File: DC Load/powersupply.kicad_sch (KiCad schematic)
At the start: 17 parts, among them IC2 LTC1046CS8#PBF, J4 DC 15V..18V, U10 MC7805BD2TR4G, U9 MC7812BD2TR4G

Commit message: Add 2.048 ref
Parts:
- added C?: 1uF, symbol Device:C_Polarized
- added C?: 10uF, symbol Device:C_Polarized
- added R?: 1K, symbol Device:R
- added R?: 470K, symbol Device:R
- added RV?: 10K, symbol Device:R_Potentiometer_Trim
- added TP?: +2.048V, symbol Connector:TestPoint
- added U?: REF5020AID, Package_SO:SOIC-8_3.9x4.9mm_P1.27mm, symbol Reference_Voltage:REF5020ID
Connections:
- net +5V: now also C?.1, U?.2 (Vin)
- new net: C?.2, C?.2, R?.1, U?.4 (GND)
- new net: R?.2, RV?.1
- new net: R?.2, RV?.2
- new net: R?.1, U?.5 (Trim/NR)
- new net +2.048V: C?.1, RV?.3, TP?.1, U?.6 (Vout)
- no-connect marks 3 -> 4

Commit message: update
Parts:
- gave numbers to parts that had none: 7
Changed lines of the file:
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@@
   (symbol (lib_id "Device:C_Polarized") (at 180.34 104.14 0) (unit 1)
     (in_bom yes) (on_board yes)
-    (property "Reference" "C?" (id 0) (at 181.61 101.6 0)
+    (property "Reference" "C10" (id 0) (at 181.61 101.6 0)
       (effects (font (size 1.27 1.27)) (justify left))
     )
@@
   (symbol (lib_id "Connector:TestPoint") (at 233.68 95.25 0) (unit 1)
     (in_bom yes) (on_board yes)
-    (property "Reference" "TP?" (id 0) (at 232.41 87.63 0)
+    (property "Reference" "TP8" (id 0) (at 232.41 87.63 0)
       (effects (font (size 1.27 1.27)) (justify left))
     )
@@
   (symbol (lib_id "Ben:+2.048V") (at 242.57 93.98 0) (unit 1)
     (in_bom yes) (on_board yes)
-    (property "Reference" "#PWR?" (id 0) (at 242.57 97.79 0)
+    (property "Reference" "#PWR09" (id 0) (at 242.57 97.79 0)
       (effects (font (size 1.27 1.27)) hide)
     )
@@
   (symbol (lib_id "Device:R") (at 228.6 115.57 180) (unit 1)
     (in_bom yes) (on_board yes)
-    (property "Reference" "R?" (id 0) (at 231.14 114.3 0))
+    (property "Reference" "R27" (id 0) (at 231.14 114.3 0))
     (property "Value" "1K" (id 1) (at 231.14 116.84 0))
     (property "Footprint" "" (id 2) (at 230.378 115.57 90)
@@
   (symbol (lib_id "Device:R_Potentiometer_Trim") (at 228.6 105.41 180) (unit 1)
     (in_bom yes) (on_board yes) (fields_autoplaced)
-    (property "Reference" "RV?" (id 0) (at 231.14 104.1399 0)
+    (property "Reference" "RV2" (id 0) (at 231.14 104.1399 0)
       (effects (font (size 1.27 1.27)) (justify right))
     )
@@
   (symbol (lib_id "Device:C_Polarized") (at 242.57 110.49 0) (unit 1)
     (in_bom yes) (on_board yes)
-    (property "Reference" "C?" (id 0) (at 243.84 107.95 0)
+    (property "Reference" "C11" (id 0) (at 243.84 107.95 0)
       (effects (font (size 1.27 1.27)) (justify left))
     )
@@
   (symbol (lib_id "power:+5V") (at 195.58 88.9 0) (unit 1)
     (in_bom yes) (on_board yes) (fields_autoplaced)
-    (property "Reference" "#PWR?" (id 0) (at 195.58 92.71 0)
+    (property "Reference" "#PWR08" (id 0) (at 195.58 92.71 0)
       (effects (font (size 1.27 1.27)) hide)
     )
@@
   (symbol (lib_id "Device:R") (at 218.44 105.41 90) (unit 1)
     (in_bom yes) (on_board yes)
-    (property "Reference" "R?" (id 0) (at 218.44 102.87 90))
+    (property "Reference" "R26" (id 0) (at 218.44 102.87 90))
     (property "Value" "470K" (id 1) (at 218.44 107.95 90))
     (property "Footprint" "" (id 2) (at 218.44 107.188 90)
@@
   (symbol (lib_id "Reference_Voltage:REF5020ID") (at 198.12 102.87 0) (unit 1)
     (in_bom yes) (on_board yes) (fields_autoplaced)
-    (property "Reference" "U?" (id 0) (at 197.5994 92.71 0)
-      (effects (font (size 1.27 1.27)) (justify left))
-    )
+    (property "Reference" "U5" (id 0) (at 197.5994 92.71 0)
+      (effects (font (size 1.27 1.27)) (justify left))
+    )

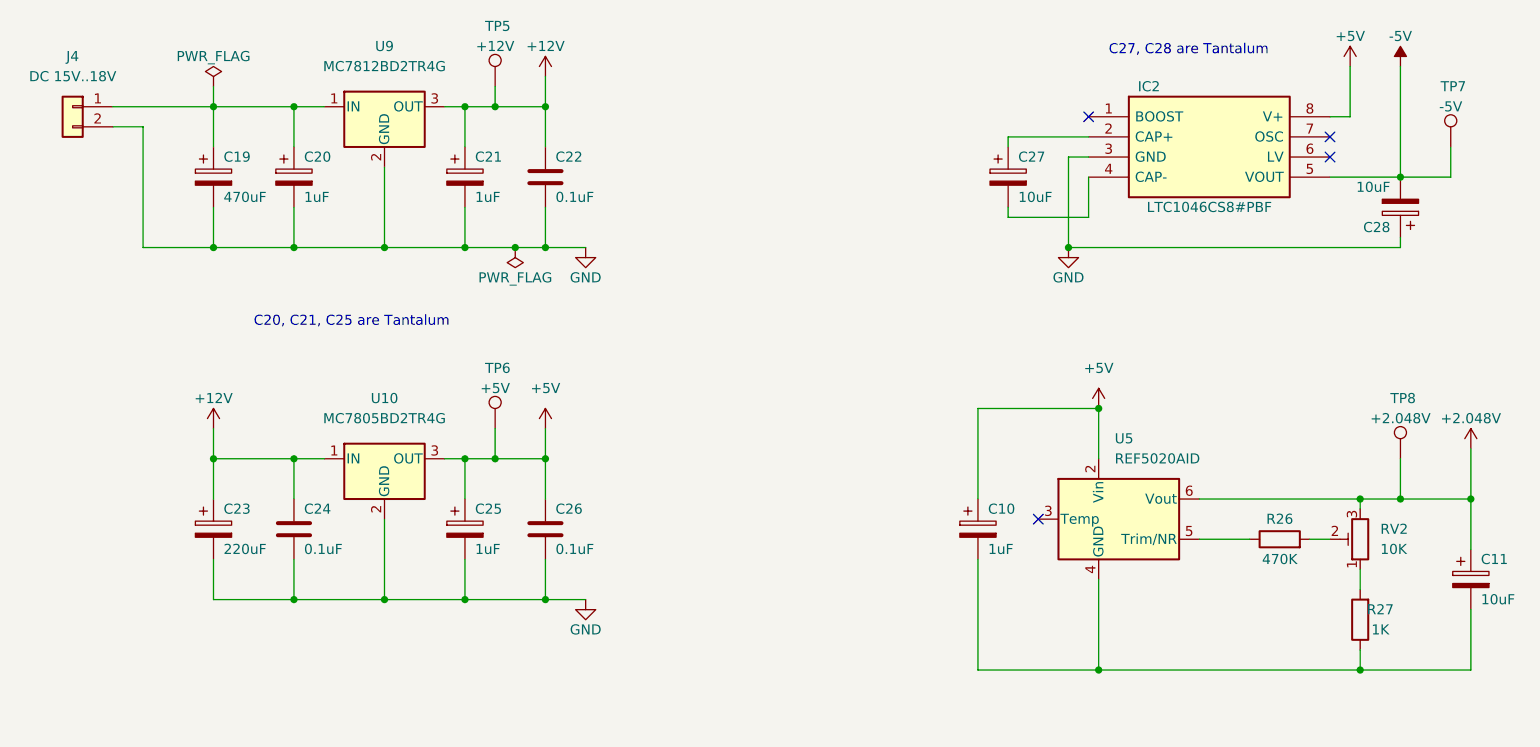
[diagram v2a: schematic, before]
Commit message: Swap to ADS131 ADC
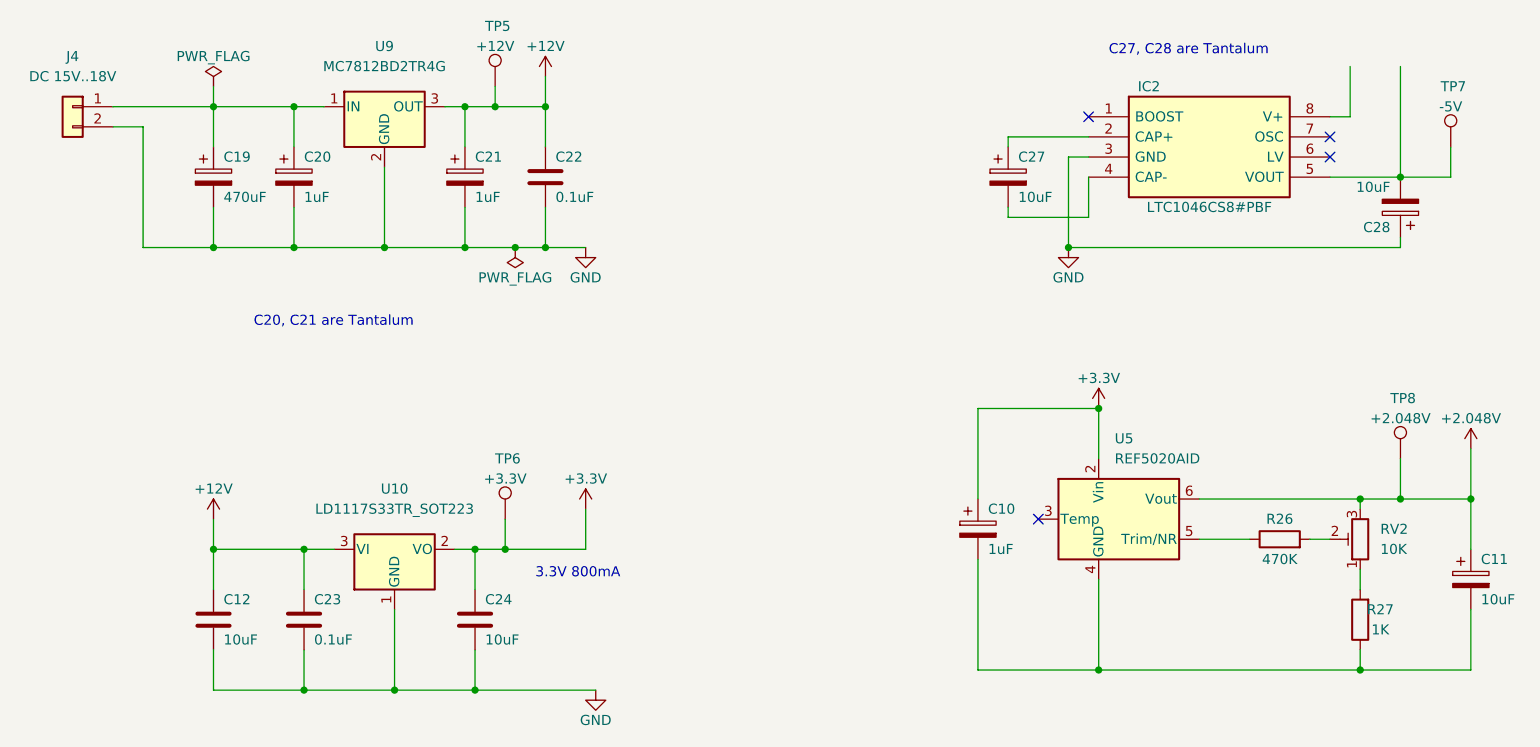
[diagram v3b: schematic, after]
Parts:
- removed C23: 220uF, symbol Device:C_Polarized
- removed C25: 1uF, symbol Device:C_Polarized
- removed C26: 0.1uF, symbol Device:C
- removed U10: MC7805BD2TR4G, Package_TO_SOT_SMD:TO-263-3_TabPin2, symbol Regulator_Linear:L7805
- added C12: 10uF, symbol Device:C
- added C23: 0.1uF, symbol Device:C
- added U10: LD1117S33TR_SOT223, Package_TO_SOT_SMD:SOT-223-3_TabPin2, symbol Regulator_Linear:LD1117S33TR_SOT223
- C24: value 0.1uF -> 10uF
- TP6: value +5V -> +3.3V
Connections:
- net +12V: now also C12.1, C23.1, U10.3 (VI); no longer C24.1
- net GND: now also C12.2, C23.2, U10.1 (GND)
- net +5V renamed +3V3
- net +3V3: now also C24.1, U10.2 (VO); no longer IC2.8 (V+)
- net -5V: no longer names the net of C28.2, IC2.5 (VOUT), TP7.1
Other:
- note added: "3.3V 800mA"
- note added: "C20, C21 are Tantalum"
- note removed: "C20, C21, C25 are Tantalum"
- moved on the sheet: TP6

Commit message: Assign temporary footprints
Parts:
- C10, C11, C12, C19, C20, C21, C22, C23, C24, C27, C28: footprint (none) -> Capacitor_SMD:C_0201_0603Metric
- IC2: footprint SOIC127P599X175-8N -> SamacSys_Parts:SOIC127P599X175-8N
- J4: footprint (none) -> Connector_PinHeader_2.54mm:PinHeader_1x02_P2.54mm_Vertical
- R26, R27: footprint (none) -> Resistor_SMD:R_0603_1608Metric
- RV2: footprint (none) -> Potentiometer_THT:Potentiometer_Bourns_3296Y_Vertical
- TP5, TP6, TP7, TP8: footprint (none) -> TestPoint:TestPoint_Loop_D2.50mm_Drill1.0mm
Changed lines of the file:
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@@
     (property "Reference" "IC2" (id 0) (at 201.93 48.26 0))
     (property "Value" "LTC1046CS8#PBF" (id 1) (at 209.55 63.5 0))
-    (property "Footprint" "SOIC127P599X175-8N" (id 2) (at 167.64 49.53 0)
+    (property "Footprint" "SamacSys_Parts:SOIC127P599X175-8N" (id 2) (at 167.64 49.53 0)
       (effects (font (size 1.27 1.27)) (justify left) hide)
     )
@@
     (property "Reference" "J4" (id 0) (at 66.04 44.45 0))
     (property "Value" "DC 15V..18V" (id 1) (at 66.04 46.99 0))
-    (property "Footprint" "" (id 2) (at 66.04 50.8 0)
+    (property "Footprint" "Connector_PinHeader_2.54mm:PinHeader_1x02_P2.54mm_Vertical" (id 2) (at 66.04 50.8 0)
       (effects (font (size 1.27 1.27)) hide)
     )
@@
       (effects (font (size 1.27 1.27)) (justify left))
     )
-    (property "Footprint" "" (id 2) (at 181.3052 107.95 0)
+    (property "Footprint" "Capacitor_SMD:C_0201_0603Metric" (id 2) (at 181.3052 107.95 0)
       (effects (font (size 1.27 1.27)) hide)
     )
@@
       (effects (font (size 1.27 1.27)) (justify left))
     )
-    (property "Footprint" "" (id 2) (at 96.2152 119.38 0)
+    (property "Footprint" "Capacitor_SMD:C_0201_0603Metric" (id 2) (at 96.2152 119.38 0)
       (effects (font (size 1.27 1.27)) hide)
     )
@@
     )
     (property "Value" "+2.048V" (id 1) (at 233.68 90.17 0))
-    (property "Footprint" "" (id 2) (at 238.76 95.25 0)
+    (property "Footprint" "TestPoint:TestPoint_Loop_D2.50mm_Drill1.0mm" (id 2) (at 238.76 95.25 0)
       (effects (font (size 1.27 1.27)) hide)
     )
@@
       (effects (font (size 1.27 1.27)) (justify left))
     )
-    (property "Footprint" "" (id 2) (at 117.8052 119.38 0)
+    (property "Footprint" "Capacitor_SMD:C_0201_0603Metric" (id 2) (at 117.8052 119.38 0)
       (effects (font (size 1.27 1.27)) hide)
     )
@@
     )
     (property "Value" "+3.3V" (id 1) (at 120.65 97.79 0))
-    (property "Footprint" "" (id 2) (at 125.73 102.87 0)
+    (property "Footprint" "TestPoint:TestPoint_Loop_D2.50mm_Drill1.0mm" (id 2) (at 125.73 102.87 0)
       (effects (font (size 1.27 1.27)) hide)
     )
@@
     )
     (property "Value" "+12V" (id 1) (at 119.38 43.18 0))
-    (property "Footprint" "" (id 2) (at 124.46 48.26 0)
+    (property "Footprint" "TestPoint:TestPoint_Loop_D2.50mm_Drill1.0mm" (id 2) (at 124.46 48.26 0)
       (effects (font (size 1.27 1.27)) hide)
     )
@@
       (effects (font (size 1.27 1.27)) (justify left))
     )
-    (property "Footprint" "" (id 2) (at 126.6952 63.5 0)
+    (property "Footprint" "Capacitor_SMD:C_0201_0603Metric" (id 2) (at 126.6952 63.5 0)
       (effects (font (size 1.27 1.27)) hide)
     )
@@
       (effects (font (size 1.27 1.27)) (justify left))
     )
-    (property "Footprint" "" (id 2) (at 116.5352 63.5 0)
+    (property "Footprint" "Capacitor_SMD:C_0201_0603Metric" (id 2) (at 116.5352 63.5 0)
       (effects (font (size 1.27 1.27)) hide)
     )
@@
       (effects (font (size 1.27 1.27)) (justify left))
     )
-    (property "Footprint" "" (id 2) (at 232.7148 59.69 0)
+    (property "Footprint" "Capacitor_SMD:C_0201_0603Metric" (id 2) (at 232.7148 59.69 0)
       (effects (font (size 1.27 1.27)) hide)
     )
@@
     (property "Reference" "R27" (id 0) (at 231.14 114.3 0))
     (property "Value" "1K" (id 1) (at 231.14 116.84 0))
-    (property "Footprint" "" (id 2) (at 230.378 115.57 90)
+    (property "Footprint" "Resistor_SMD:R_0603_1608Metric" (id 2) (at 230.378 115.57 90)
       (effects (font (size 1.27 1.27)) hide)
     )
@@
       (effects (font (size 1.27 1.27)) (justify right))
     )
-    (property "Footprint" "" (id 2) (at 228.6 105.41 0)
+    (property "Footprint" "Potentiometer_THT:Potentiometer_Bourns_3296Y_Vertical" (id 2) (at 228.6 105.41 0)
       (effects (font (size 1.27 1.27)) hide)
     )
@@
       (effects (font (size 1.27 1.27)) (justify left))
     )
-    (property "Footprint" "" (id 2) (at 243.5352 114.3 0)
+    (property "Footprint" "Capacitor_SMD:C_0201_0603Metric" (id 2) (at 243.5352 114.3 0)
       (effects (font (size 1.27 1.27)) hide)
     )
@@
     )
     (property "Value" "-5V" (id 1) (at 240.03 50.8 0))
-    (property "Footprint" "" (id 2) (at 245.11 55.88 0)
+    (property "Footprint" "TestPoint:TestPoint_Loop_D2.50mm_Drill1.0mm" (id 2) (at 245.11 55.88 0)
       (effects (font (size 1.27 1.27)) hide)
     )
@@
     (property "Reference" "R26" (id 0) (at 218.44 102.87 90))
     (property "Value" "470K" (id 1) (at 218.44 107.95 90))
-    (property "Footprint" "" (id 2) (at 218.44 107.188 90)
+    (property "Footprint" "Resistor_SMD:R_0603_1608Metric" (id 2) (at 218.44 107.188 90)
       (effects (font (size 1.27 1.27)) hide)
     )
@@
       (effects (font (size 1.27 1.27)) (justify left))
     )
-    (property "Footprint" "" (id 2) (at 185.1152 63.5 0)
+    (property "Footprint" "Capacitor_SMD:C_0201_0603Metric" (id 2) (at 185.1152 63.5 0)
       (effects (font (size 1.27 1.27)) hide)
     )
@@
       (effects (font (size 1.27 1.27)) (justify left))
     )
-    (property "Footprint" "" (id 2) (at 94.9452 63.5 0)
+    (property "Footprint" "Capacitor_SMD:C_0201_0603Metric" (id 2) (at 94.9452 63.5 0)
       (effects (font (size 1.27 1.27)) hide)
     )
@@
       (effects (font (size 1.27 1.27)) (justify left))
     )
-    (property "Footprint" "" (id 2) (at 84.7852 63.5 0)
+    (property "Footprint" "Capacitor_SMD:C_0201_0603Metric" (id 2) (at 84.7852 63.5 0)
       (effects (font (size 1.27 1.27)) hide)
     )
@@
       (effects (font (size 1.27 1.27)) (justify left))
     )
-    (property "Footprint" "" (id 2) (at 84.7852 119.38 0)
-      (effects (font (size 1.27 1.27)) hide)
-    )
+    (property "Footprint" "Capacitor_SMD:C_0201_0603Metric" (id 2) (at 84.7852 119.38 0)
+      (effects (font (size 1.27 1.27)) hide)
+    )
